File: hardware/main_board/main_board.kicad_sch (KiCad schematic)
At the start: 4 parts

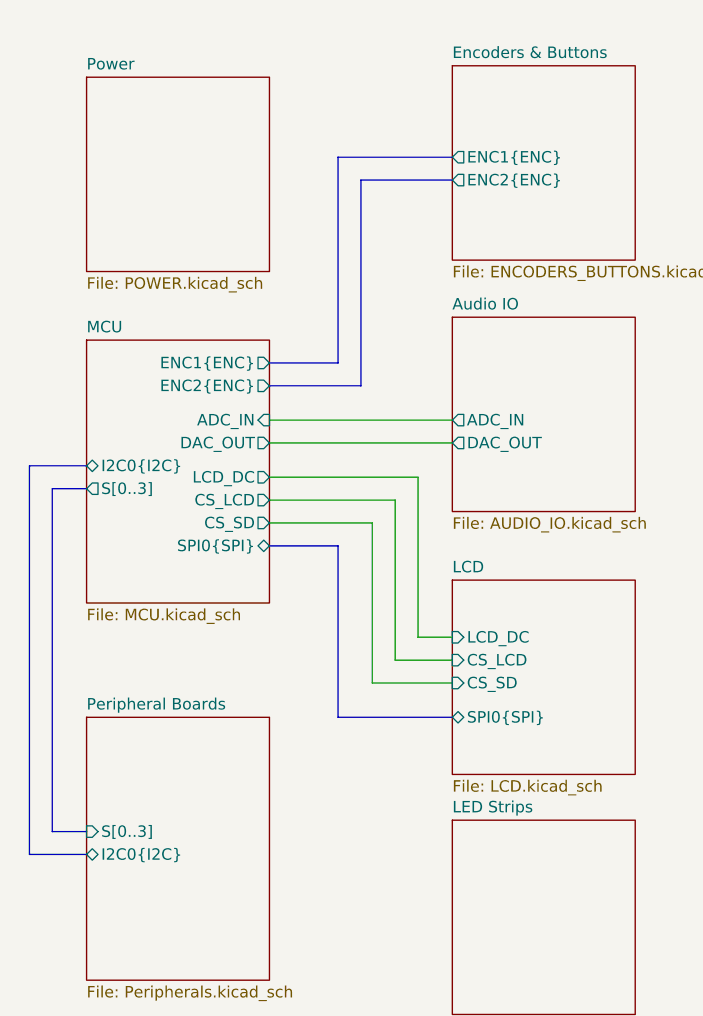
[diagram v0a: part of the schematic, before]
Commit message: fixed peripheral board dimensions to be compatible with 2.54 mm pitch protoboard for daisy chaining. deleted gerbers. added some more content to main board (wip)
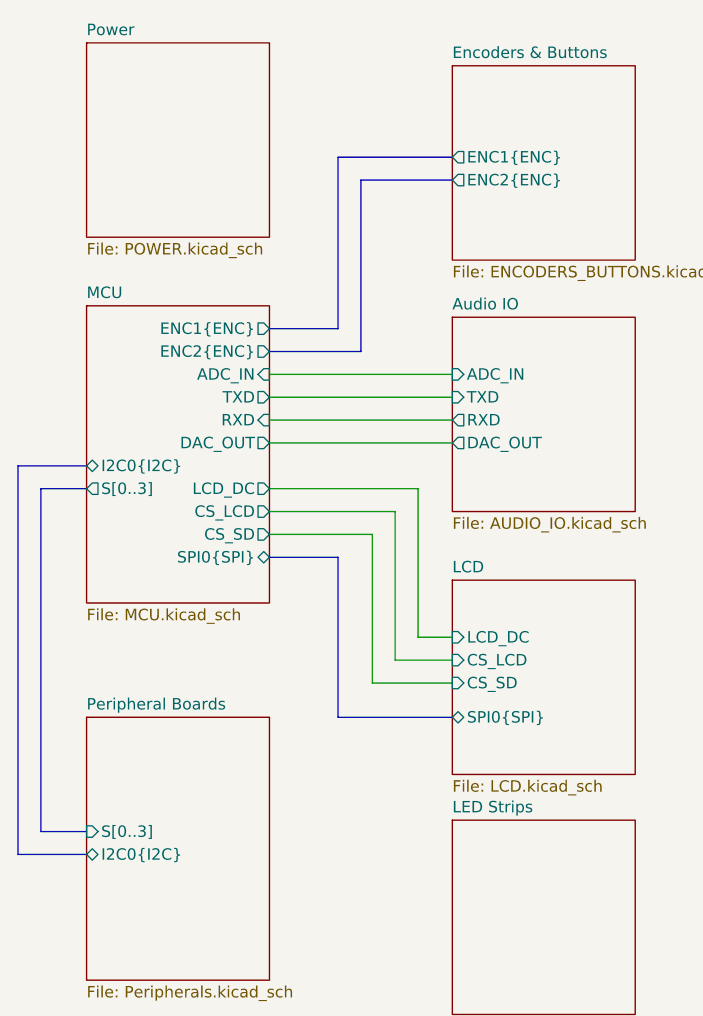
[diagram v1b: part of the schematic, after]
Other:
- sheet Audio IO ports: added RXD, TXD; removed none
- sheet MCU ports: added RXD, TXD; removed none
